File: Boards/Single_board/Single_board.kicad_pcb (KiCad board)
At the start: 2 copper layers, 169.9 x 190.9 mm, 74 parts, among them J1 POWER, J2 ICSP, J3 USB_C_Receptacle_USB2.0_16P, SW1 +, SW10 5, SW11 2, SW12 9, SW13 PRO, SW14 6, SW15 3, SW16 CLR, SW17 ENTR, SW18 RSET, SW19 KEYREL, SW2 VERB, SW3 NOUN, SW4 0, SW5 7, SW6 -, SW7 4, SW8 1, SW9 8, U2 ATmega328P-A, U3 CH340C

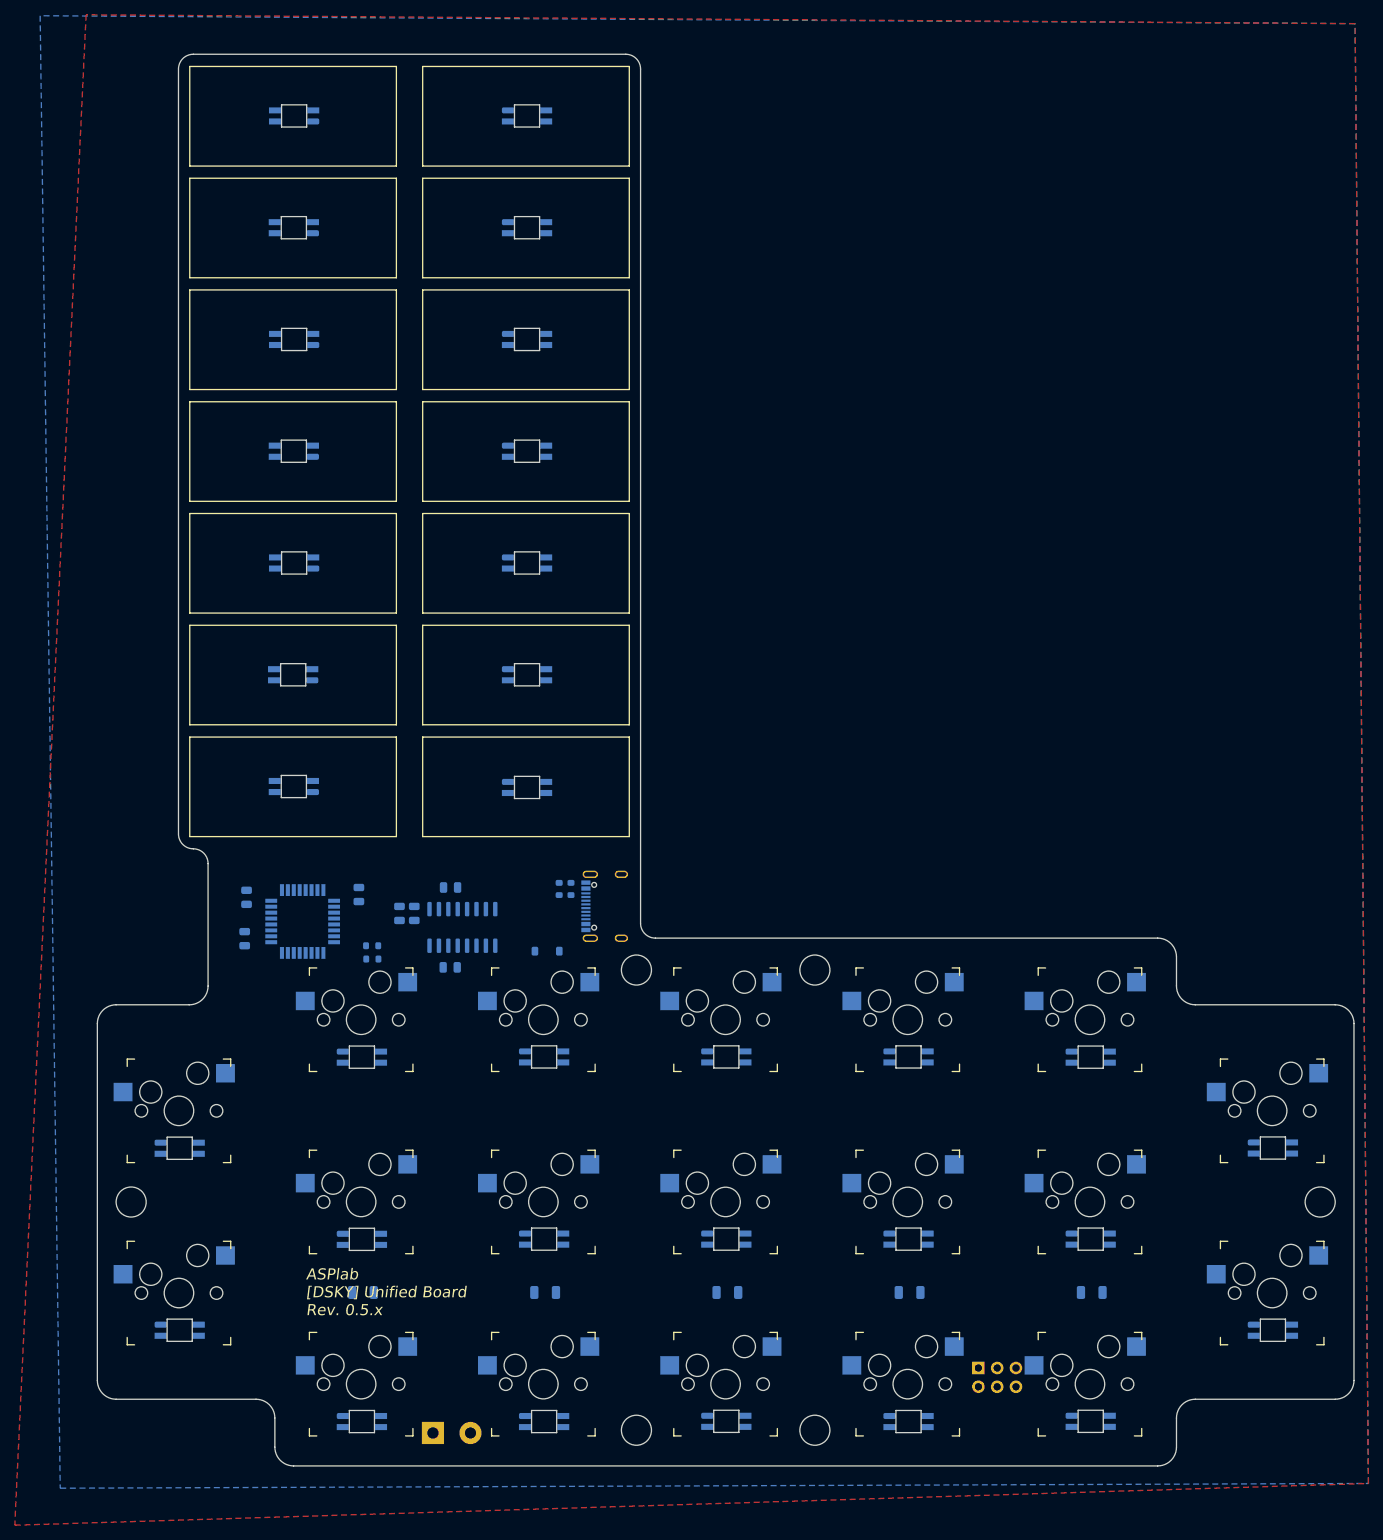
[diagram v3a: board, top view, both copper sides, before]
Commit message: Arrange and place components
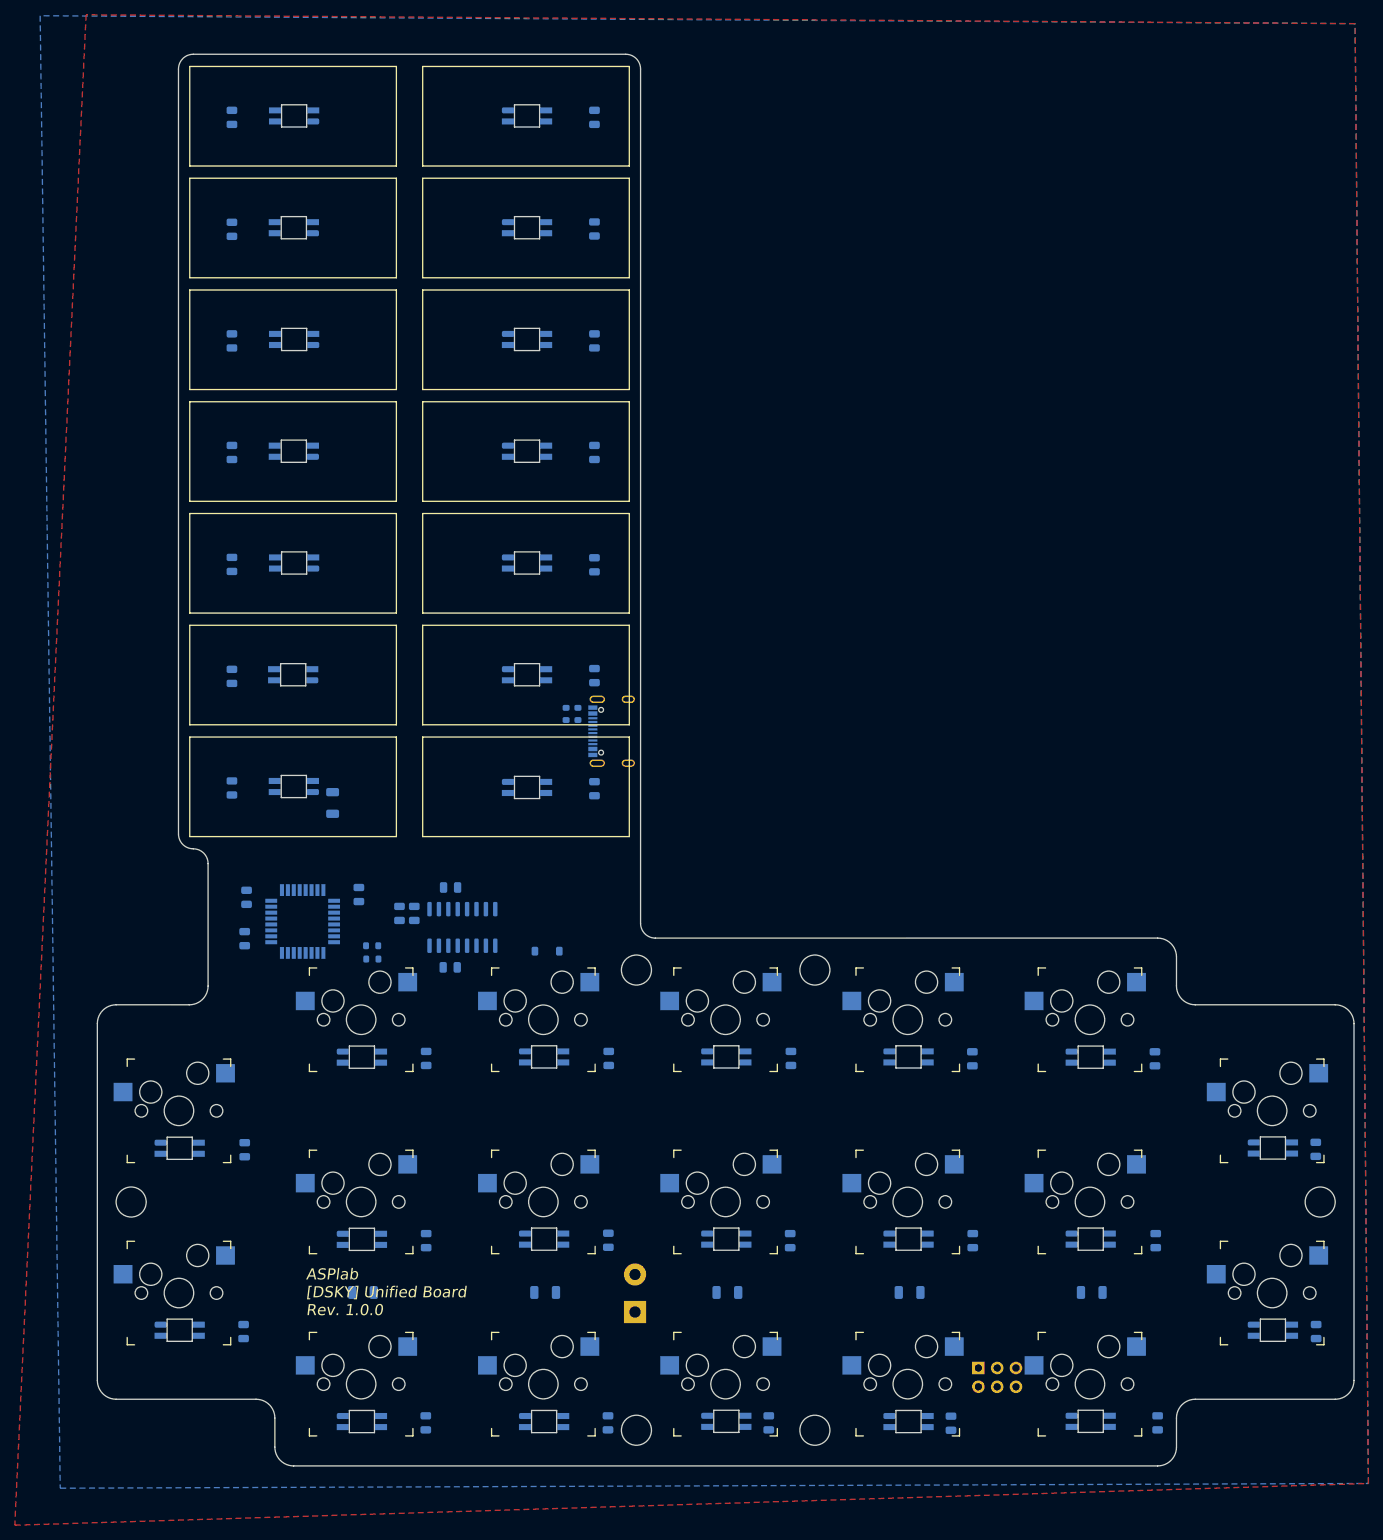
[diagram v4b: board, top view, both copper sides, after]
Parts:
- added C10: 100nF, Capacitor_SMD:C_0805_2012Metric, B.Cu at (140.9, 119.9)
- added C11: 100nF, Capacitor_SMD:C_0805_2012Metric, B.Cu at (189.9, 119.8)
- added C12: 100nF, Capacitor_SMD:C_0805_2012Metric, B.Cu at (140.9, 104.7)
- added C13: 100nF, Capacitor_SMD:C_0805_2012Metric, B.Cu at (189.9, 104.8)
- added C14: 100nF, Capacitor_SMD:C_0805_2012Metric, B.Cu at (140.9, 89.6)
- added C15: 100nF, Capacitor_SMD:C_0805_2012Metric, B.Cu at (189.9, 89.6)
- added C16: 100nF, Capacitor_SMD:C_0805_2012Metric, B.Cu at (140.9, 74.5)
- added C17: 100nF, Capacitor_SMD:C_0805_2012Metric, B.Cu at (189.9, 74.5)
- added C18: 100nF, Capacitor_SMD:C_0805_2012Metric, B.Cu at (140.9, 59.4)
- added C19: 100nF, Capacitor_SMD:C_0805_2012Metric, B.Cu at (189.9, 59.4)
- added C20: 100nF, Capacitor_SMD:C_0805_2012Metric, B.Cu at (140.9, 44.3)
- added C21: 100nF, Capacitor_SMD:C_0805_2012Metric, B.Cu at (189.9, 44.3)
- added C22: 100nF, Capacitor_SMD:C_0805_2012Metric, B.Cu at (142.6, 183.9)
- added C23: 100nF, Capacitor_SMD:C_0805_2012Metric, B.Cu at (142.5, 208.5)
- added C24: 100nF, Capacitor_SMD:C_0805_2012Metric, B.Cu at (167.2, 171.5)
- added C25: 100nF, Capacitor_SMD:C_0805_2012Metric, B.Cu at (167.2, 196.2)
- added C26: 100nF, Capacitor_SMD:C_0805_2012Metric, B.Cu at (167.1, 220.8)
- added C27: 100nF, Capacitor_SMD:C_0805_2012Metric, B.Cu at (191.9, 171.5)
- added C28: 100nF, Capacitor_SMD:C_0805_2012Metric, B.Cu at (191.8, 196.1)
- added C29: 100nF, Capacitor_SMD:C_0805_2012Metric, B.Cu at (191.8, 220.8)
- added C30: 100nF, Capacitor_SMD:C_0805_2012Metric, B.Cu at (216.5, 171.5)
- added C31: 100nF, Capacitor_SMD:C_0805_2012Metric, B.Cu at (216.4, 196.2)
- added C32: 100nF, Capacitor_SMD:C_0805_2012Metric, B.Cu at (213.5, 220.8)
- added C33: 100nF, Capacitor_SMD:C_0805_2012Metric, B.Cu at (241.0, 171.6)
- added C34: 100nF, Capacitor_SMD:C_0805_2012Metric, B.Cu at (241.1, 196.2)
- added C35: 100nF, Capacitor_SMD:C_0805_2012Metric, B.Cu at (238.2, 220.9)
- added C36: 100nF, Capacitor_SMD:C_0805_2012Metric, B.Cu at (265.7, 171.6)
- added C37: 100nF, Capacitor_SMD:C_0805_2012Metric, B.Cu at (265.8, 196.2)
- added C38: 100nF, Capacitor_SMD:C_0805_2012Metric, B.Cu at (266.1, 220.8)
- added C39: 100nF, Capacitor_SMD:C_0805_2012Metric, B.Cu at (287.5, 183.8)
- added C40: 100nF, Capacitor_SMD:C_0805_2012Metric, B.Cu at (287.5, 208.5)
- added C8: 100nF, Capacitor_SMD:C_0805_2012Metric, B.Cu at (140.9, 135.0)
- added C9: 100nF, Capacitor_SMD:C_0805_2012Metric, B.Cu at (189.9, 135.1)
- added R1: 500, Resistor_SMD:R_1206_3216Metric, B.Cu at (154.5, 137.0)
- C5: renamed from C3; value 100nF -> 4.7uF
- C6: renamed from C4; value 4.7uF -> 100nF
- moved J1 31.9 mm to (195.4, 205.8), turned to 90 degrees
- moved J3 23.7 mm to (193.4, 127.3)
- moved R44 23.7 mm to (187.7, 124.9)
- moved R45 23.7 mm to (186.1, 124.9)
- renumbered C6 to C1, C7 to C2, C8 to C3, C9 to C4, C5 to C7, D33 to D1, D22 to D10, D28 to D11, D21 to D12, D27 to D13, D20 to D14, D18 to D15, D19 to D16, D15 to D17, D16 to D18, D17 to D19, D26 to D2, D12 to D20, D13 to D21, D14 to D22, D9 to D23, D10 to D24, D11 to D25, D6 to D26, D7 to D27, D8 to D28, D3 to D29, D32 to D3, D4 to D30, D5 to D31, D1 to D32, D2 to D33, D25 to D4, D31 to D5, D24 to D6, D30 to D7, D23 to D8, D29 to D9
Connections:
- D1 pad 1: unconnected-(D33-DOUT-Pad1) -> Net-(D1-DOUT)
- D1 pad 3: Net-(D31-DOUT) -> Net-(D1-DIN)
- D10 pad 1: Net-(D22-DOUT) -> Net-(D10-DOUT)
- D10 pad 2: unconnected-(D22-VSS-Pad2) -> GND
- D10 pad 3: Net-(D20-DOUT) (its old number) -> Net-(D10-DIN)
- D11 pad 1: Net-(D28-DOUT) -> Net-(D11-DOUT)
- D11 pad 2: unconnected-(D28-VSS-Pad2) -> GND
- D11 pad 3: Net-(D26-DOUT) (its old number) -> Net-(D10-DOUT)
- D12 pad 1: Net-(D21-DOUT) (its old number) -> Net-(D12-DOUT)
- D12 pad 3: Net-(D21-DIN) -> Net-(D11-DOUT)
- D13 pad 1: Net-(D27-DOUT) (its old number) -> Net-(D13-DOUT)
- D13 pad 3: Net-(D25-DOUT) -> Net-(D12-DOUT)
- D14 pad 1: Net-(D20-DOUT) (its old number) -> Net-(D14-DOUT)
- D14 pad 2: unconnected-(D20-VSS-Pad2) -> GND
- D14 pad 3: Net-(D19-DOUT) -> Net-(D13-DOUT)
- D15 pad 3: Net-(D17-DOUT) (its old number) -> Net-(D14-DOUT)
- D16 pad 1: Net-(D19-DOUT) -> Net-(D16-DOUT)
- D17 pad 3: Net-(D14-DOUT) -> Net-(D16-DOUT)
- D19 pad 1: Net-(D17-DOUT) (its old number) -> Net-(D19-DOUT)
- D2 pad 1: Net-(D26-DOUT) (its old number) -> Net-(D2-DOUT)
- D2 pad 2: unconnected-(D26-VSS-Pad2) -> GND
- D2 pad 3: Net-(D24-DOUT) (its old number) -> Net-(D1-DOUT)
- D20 pad 3: Net-(D11-DOUT) -> Net-(D19-DOUT)
- D22 pad 1: Net-(D14-DOUT) -> Net-(D22-DOUT)
- D23 pad 2: unconnected-(D9-VSS-Pad2) -> GND
- D23 pad 3: Net-(D8-DOUT) -> Net-(D22-DOUT)
- D24 pad 2: unconnected-(D10-VSS-Pad2) -> GND
- D25 pad 1: Net-(D11-DOUT) -> Net-(D25-DOUT)
- D26 pad 2: unconnected-(D6-VSS-Pad2) -> GND
- D26 pad 3: Net-(D5-DOUT) -> Net-(D25-DOUT)
- D27 pad 2: unconnected-(D7-VSS-Pad2) -> GND
- D28 pad 1: Net-(D8-DOUT) -> Net-(D28-DOUT)
- D28 pad 2: unconnected-(D8-VSS-Pad2) -> GND
- D29 pad 2: unconnected-(D3-VSS-Pad2) -> GND
- D29 pad 3: Net-(D2-DOUT) -> Net-(D28-DOUT)
- D3 pad 1: Net-(D21-DIN) -> Net-(D3-DOUT)
- D3 pad 2: unconnected-(D32-VSS-Pad2) -> GND
- D3 pad 3: Net-(D30-DOUT) (its old number) -> Net-(D2-DOUT)
- D30 pad 2: unconnected-(D4-VSS-Pad2) -> GND
- D31 pad 1: Net-(D5-DOUT) -> Net-(D31-DOUT)
- D31 pad 2: unconnected-(D5-VSS-Pad2) -> GND
- D32 pad 2: unconnected-(D1-VSS-Pad2) -> GND
- D32 pad 3: RGB_DIN -> Net-(D31-DOUT)
- D33 pad 1: Net-(D2-DOUT) -> unconnected-(D33-DOUT-Pad1)
- D33 pad 2: unconnected-(D2-VSS-Pad2) -> GND
- D4 pad 1: Net-(D25-DOUT) -> Net-(D4-DOUT)
- D4 pad 3: Net-(D23-DOUT) (its old number) -> Net-(D3-DOUT)
- D5 pad 1: Net-(D31-DOUT) -> Net-(D5-DOUT)
- D5 pad 3: Net-(D29-DOUT) (its old number) -> Net-(D4-DOUT)
- D6 pad 1: Net-(D24-DOUT) (its old number) -> Net-(D6-DOUT)
- D6 pad 2: unconnected-(D24-VSS-Pad2) -> GND
- D6 pad 3: Net-(D22-DOUT) -> Net-(D5-DOUT)
- D7 pad 1: Net-(D30-DOUT) (its old number) -> Net-(D7-DOUT)
- D7 pad 2: unconnected-(D30-VSS-Pad2) -> GND
- D7 pad 3: Net-(D28-DOUT) -> Net-(D6-DOUT)
- D8 pad 1: Net-(D23-DOUT) (its old number) -> Net-(D8-DOUT)
- D8 pad 3: Net-(D21-DOUT) (its old number) -> Net-(D7-DOUT)
- D9 pad 1: Net-(D29-DOUT) (its old number) -> Net-(D10-DIN)
- D9 pad 3: Net-(D27-DOUT) (its old number) -> Net-(D8-DOUT)
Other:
- board text added: "ASPlab [DSKY] Unified Board Rev. 1.0.0"
- board text removed: "ASPlab [DSKY] Unified Board Rev. 0.5.x"

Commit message: Add usb ports and separate power sources. Pending fitting test.
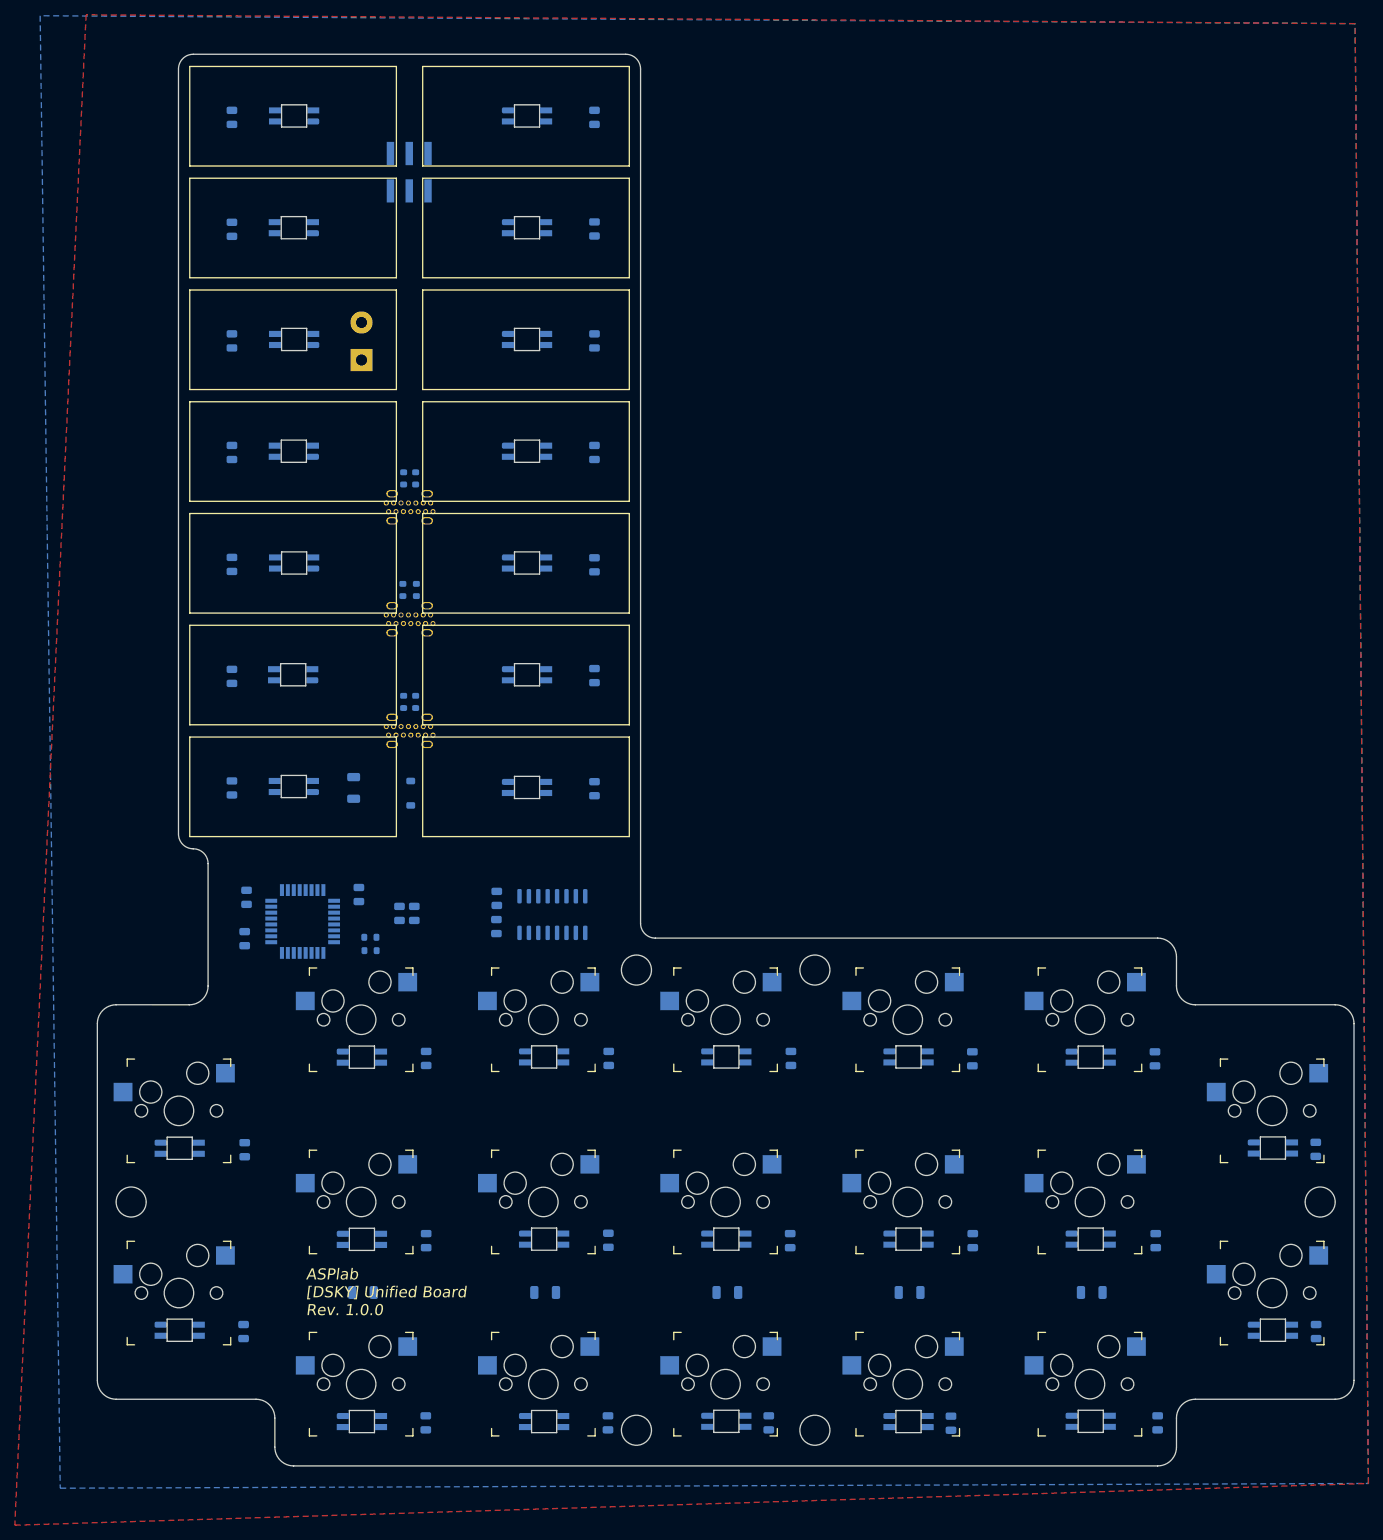
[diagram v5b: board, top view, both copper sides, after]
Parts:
- added J4: USB_C_Receptacle_USB2.0_16P, Project Libraries:USB-C-TH_918-468K2029E50001, B.Cu at (164.9, 112.1)
- added J5: USB_C_Receptacle_USB2.0_16P, Project Libraries:USB-C-TH_918-468K2029E50001, B.Cu at (164.9, 97.0)
- added R10: 5.1k, Resistor_SMD:R_0603_1608Metric, B.Cu at (164.1, 93.1)
- added R2: 5.1k, Resistor_SMD:R_0603_1608Metric, B.Cu at (164.0, 108.2)
- added R3: 5.1k, Resistor_SMD:R_0603_1608Metric, B.Cu at (165.9, 108.2)
- added R9: 5.1k, Resistor_SMD:R_0603_1608Metric, B.Cu at (165.8, 93.1)
- J2: footprint Connector_PinHeader_2.54mm:PinHeader_2x03_P2.54mm_Horizontal -> Connector_PinHeader_2.54mm:PinHeader_2x03_P2.54mm_Vertical_SMD
- J3: footprint Connector_USB:USB_C_Receptacle_G-Switch_GT-USB-7010ASV -> Project Libraries:USB-C-TH_918-468K2029E50001
- moved J2 179.1 mm to (164.9, 51.7)
- moved J1 133.9 mm to (158.4, 77.1)
- moved J3 28.5 mm to (164.9, 127.2)
- moved D34 28.2 mm to (165.1, 135.7), turned to 90 degrees
- moved R44 23.6 mm to (164.1, 123.3)
- moved R45 20.4 mm to (165.8, 123.3)
- moved U3 12.3 mm to (184.3, 152.1)
- moved C3 8.33 mm to (176.7, 153.7), turned to -90 degrees
- moved C4 6.42 mm to (176.7, 149.9), turned to -90 degrees
- moved R1 3.50 mm to (157.4, 135.0)
- moved R46 1.16 mm to (159.6, 155.1)
- moved R47 1.16 mm to (159.7, 156.9)
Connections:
- C1 pad 1: +5V -> 5V1A
- C10 pad 2: +5V -> 5V10A
- C11 pad 2: +5V -> 5V10A
- C12 pad 2: +5V -> 5V10A
- C13 pad 2: +5V -> 5V10A
- C14 pad 2: +5V -> 5V10A
- C15 pad 2: +5V -> 5V10A
- C16 pad 2: +5V -> 5V10A
- C17 pad 2: +5V -> 5V10A
- C18 pad 2: +5V -> 5V10A
- C19 pad 2: +5V -> 5V10A
- C2 pad 1: +5V -> 5V1A
- C20 pad 2: +5V -> 5V10A
- C21 pad 2: +5V -> 5V10A
- C22 pad 2: +5V -> 5V10A
- C23 pad 2: +5V -> 5V10A
- C24 pad 2: +5V -> 5V10A
- C25 pad 2: +5V -> 5V10A
- C26 pad 2: +5V -> 5V10A
- C27 pad 2: +5V -> 5V10A
- C28 pad 2: +5V -> 5V10A
- C29 pad 2: +5V -> 5V10A
- C30 pad 2: +5V -> 5V10A
- C31 pad 2: +5V -> 5V10A
- C32 pad 2: +5V -> 5V10A
- C33 pad 2: +5V -> 5V10A
- C34 pad 2: +5V -> 5V10A
- C35 pad 2: +5V -> 5V10A
- C36 pad 2: +5V -> 5V10A
- C37 pad 2: +5V -> 5V10A
- C38 pad 2: +5V -> 5V10A
- C39 pad 2: +5V -> 5V10A
- C40 pad 2: +5V -> 5V10A
- C5 pad 1: +5V -> 5V1A
- C6 pad 1: +5V -> 5V1A
- C8 pad 2: +5V -> 5V10A
- C9 pad 2: +5V -> 5V10A
- D1 pad 4: +5V -> 5V10A
- D10 pad 4: +5V -> 5V10A
- D11 pad 4: +5V -> 5V10A
- D12 pad 4: +5V -> 5V10A
- D13 pad 4: +5V -> 5V10A
- D14 pad 4: +5V -> 5V10A
- D15 pad 4: +5V -> 5V10A
- D16 pad 4: +5V -> 5V10A
- D17 pad 4: +5V -> 5V10A
- D18 pad 4: +5V -> 5V10A
- D19 pad 4: +5V -> 5V10A
- D2 pad 4: +5V -> 5V10A
- D20 pad 4: +5V -> 5V10A
- D21 pad 4: +5V -> 5V10A
- D22 pad 4: +5V -> 5V10A
- D23 pad 4: +5V -> 5V10A
- D24 pad 4: +5V -> 5V10A
- D25 pad 4: +5V -> 5V10A
- D26 pad 4: +5V -> 5V10A
- D27 pad 4: +5V -> 5V10A
- D28 pad 4: +5V -> 5V10A
- D29 pad 4: +5V -> 5V10A
- D3 pad 4: +5V -> 5V10A
- D30 pad 4: +5V -> 5V10A
- D31 pad 4: +5V -> 5V10A
- D32 pad 4: +5V -> 5V10A
- D33 pad 4: +5V -> 5V10A
- D34 pad 1: +5V -> 5V1A
- D4 pad 4: +5V -> 5V10A
- D5 pad 4: +5V -> 5V10A
- D6 pad 4: +5V -> 5V10A
- D7 pad 4: +5V -> 5V10A
- D8 pad 4: +5V -> 5V10A
- D9 pad 4: +5V -> 5V10A
- J1 pad 2: +5V -> 5V10A
- J2 pad 2: +5V -> 5V1A
- U2 pad 18: +5V -> 5V1A
- U2 pad 4: +5V -> 5V1A
- U2 pad 6: +5V -> 5V1A
- U3 pad 16: +5V -> 5V1A
